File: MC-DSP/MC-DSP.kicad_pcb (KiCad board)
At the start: 2 copper layers, 173 parts, among them J80 5-1634513-1, J81 5-1634513-1, J82 5-1634513-1, SW1 SW_SPDT, U1 TMS320F28388DZWT, U10 ECS-2520MV-xxx-xx, U12 BU4831F-TR, U13 BU4811G-TR, U2 SBH41-NBPB-D10-ST-BK, U20 R-78E3.3-1.0, U200 FT2232HL, U201 TPD2S017, U202 USB_B, U203 AZ1117-3.3, U204 ISO7730DW, U205 ISO7730DW, U206 ISO7730DW, U21 R-78B1.2-2.0, U60 OPA365xxD, U61 OPA365xxD, U62 OPA365xxD, U63 OPA365xxD, U64 OPA365xxD, U65 MAX6126AASA, U80 OPA365xxD, U81 OPA365xxD, U82 OPA365xxD

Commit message: added backplane connector, changed right angle headers, added FP for bigger reg caps, all ICs arranged, routed isolated section.
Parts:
- removed D11, D12: WP1384AD/YD, LED_THT:LED_D3.0mm
- removed R11, R12: 1K, Resistor_SMD:R_0603_1608Metric_Pad0.98x0.95mm_HandSolder
- removed R13: 44R, Resistor_SMD:R_0603_1608Metric_Pad0.98x0.95mm_HandSolder
- removed R14, R15, R16, R17: 10R, Resistor_SMD:R_0603_1608Metric_Pad0.98x0.95mm_HandSolder
- added H2: Conn_01x05, Connector_PinSocket_2.54mm:PinSocket_1x05_P2.54mm_Vertical, F.Cu at (251.2, 23.6)
- added H3: Conn_01x05, Connector_PinSocket_2.54mm:PinSocket_1x05_P2.54mm_Vertical, F.Cu at (253.7, 23.6)
- added J1: 374385, 374385:374385, F.Cu at (113.9, 101.1)
- added U207: Crystal_GND24, Oscillator:Oscillator_SMD_TXC_7C-4Pin_5.0x3.2mm_HandSoldering, F.Cu at (233.6, 105.7)
- C21, C22, C28: footprint Capacitor_SMD:C_0603_1608Metric_Pad1.08x0.95mm_HandSolder -> Capacitor_SMD:C_1210_3225Metric
- H1: value Conn_02x12_Odd_Even -> Conn_01x05; footprint Connector_PinHeader_1.27mm:PinHeader_2x12_P1.27mm_Vertical -> Connector_PinSocket_2.54mm:PinSocket_1x05_P2.54mm_Vertical
- moved U12 391.6 mm to (178.1, 25.1), turned to 270 degrees
- moved C14 384.6 mm to (178.1, 27.7)
- moved C16 378.6 mm to (178.1, 31.2), turned to 180 degrees
- moved R18 377.2 mm to (178.1, 29.5)
- moved U13 369.0 mm to (178.1, 35.3)
- moved C15 362.0 mm to (178.1, 38.6)
- moved R21 351.4 mm to (167.8, 33.2)
- moved R20 349.4 mm to (160.3, 20.0), turned to 180 degrees
- moved U21 346.7 mm to (156.6, 34.6)
- moved C22 345.3 mm to (140.7, 23.0), turned to 270 degrees
- moved L22 345.2 mm to (168.1, 35.4), turned to 180 degrees
- moved C28 344.4 mm to (141.1, 39.1), turned to 90 degrees
- moved C30 344.4 mm to (166.9, 38.6), turned to 90 degrees
- moved C31 344.2 mm to (169.4, 38.6), turned to 270 degrees
- moved L24 342.9 mm to (148.0, 39.3), turned to 90 degrees
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- renumbered TP1 to T1
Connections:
- net /Ethernet/COL renamed Net-(U1-PadM2)
- net /Ethernet/CRS renamed Net-(U1-PadN2)
- net /Ethernet/MDC renamed Net-(U1-PadJ3)
- net /Ethernet/MDIO renamed Net-(U1-PadL2)
- net /Ethernet/PWDN renamed Net-(U1-PadL4)
- net /Ethernet/RX_CLK renamed Net-(U1-PadM4)
- net /Ethernet/RX_D0 renamed Net-(U1-PadN3)
- net /Ethernet/RX_D1 renamed Net-(U1-PadV12)
- net /Ethernet/RX_D2 renamed Net-(U1-PadW10)
- net /Ethernet/RX_D3 renamed Net-(U1-PadU12)
- net /Ethernet/RX_DV renamed Net-(U1-PadM3)
- net /Ethernet/RX_ER renamed Net-(U1-PadN4)
- net /Ethernet/Reset renamed Net-(U1-PadT15)
- net /Ethernet/TX_CLK renamed Net-(U1-PadU15)
- net /Ethernet/TX_D0 renamed Net-(U1-PadW16)
- net /Ethernet/TX_D1 renamed Net-(U1-PadT8)
- net /Ethernet/TX_D2 renamed Net-(U1-PadU8)
- net /Ethernet/TX_D3 renamed Net-(U1-PadV8)
- net /Ethernet/TX_EN renamed Net-(U1-PadT12)
- C13 pad 1: +3V3 -> GND
- C13 pad 2: GND -> +3V3
- C200 pad 2: GND -> EMU_GND
- C201 pad 2: GND -> EMU_GND
- C202 pad 2: GND -> EMU_GND
- C203 pad 2: GND -> EMU_GND
- C204 pad 2: GND -> EMU_GND
- C205 pad 2: GND -> EMU_GND
- C206 pad 2: GND -> EMU_GND
- C207 pad 2: GND -> EMU_GND
- C208 pad 2: GND -> EMU_GND
- C209 pad 2: GND -> EMU_GND
- H1 pad 2: /CLB_OUTPUTX_BAR8 -> /OUTPUTXBAR2
- H1 pad 3: /OUTPUTXBAR2 -> GND
- H1 pad 4: /CLB_OUTPUTX_BAR7 -> /OUTPUTXBAR3
- H1 pad 5: /OUTPUTXBAR3 -> /OUTPUTXBAR4
- R109 pad 1: CLK_25M_DSP -> /25MHz_clk_DSP
- U1 pad G19: CLK_25M_DSP -> /25MHz_clk_DSP
- U10 pad 3: Net-(U10-Pad3) -> /25MHz_clk_DSP
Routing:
- net EMU_GND: track 0.00 -> 53.9 mm, vias 0 -> 26
- net Net-(JP201-Pad2): track 0.00 -> 30.7 mm, vias 0 -> 2
- net EMU_3V3: track 0.00 -> 29.5 mm, vias 0 -> 16
- net /FTDI/EMU_TCK: track 0.00 -> 28.7 mm, vias 0 -> 1
- net /FTDI/EMU_SCI-TX: track 0.00 -> 26.6 mm, vias 0 -> 2
- net /FTDI/EMU_TDI: track 0.00 -> 26.0 mm, vias 0 -> 2
- net Net-(JP200-Pad2): track 0.00 -> 24.3 mm, vias 0 -> 2
- net /FTDI/EMU_TMS: track 0.00 -> 24.0 mm, vias 0 -> 2
- net /FTDI/EMU_SCI-RX: track 0.00 -> 17.0 mm, vias 0 -> 2
- net /FTDI/EMU_TDO: track 0.00 -> 16.4 mm, vias 0 -> 2
- net EMU_1V8: track 0.00 -> 16.0 mm, vias 0 -> 4
- net Net-(R201-Pad1): track 0.00 -> 15.1 mm
- net /FTDI/EMU_TRSTn: track 0.00 -> 11.6 mm, vias 0 -> 2
- net Net-(R205-Pad2): track 0.00 -> 10.4 mm
- net EMU_USB_5V: track 0.00 -> 10.4 mm
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- added copper zone on B.Cu, net EMU_1V8
- added copper zone on In2.Cu, net EMU_3V3
- added copper zone on In3.Cu, net EMU_5V
- added copper zone on In1.Cu, net EMU_GND
- added copper zone on In4.Cu, net EMU_GND
- added copper zone on In1.Cu, net GND
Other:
- board outline added: 160 x 100 mm
- copper layers 2 -> 6
- rule trace_min: 0.2 -> 0.1524
- rule via_min_size: 0.4 -> 0.2032

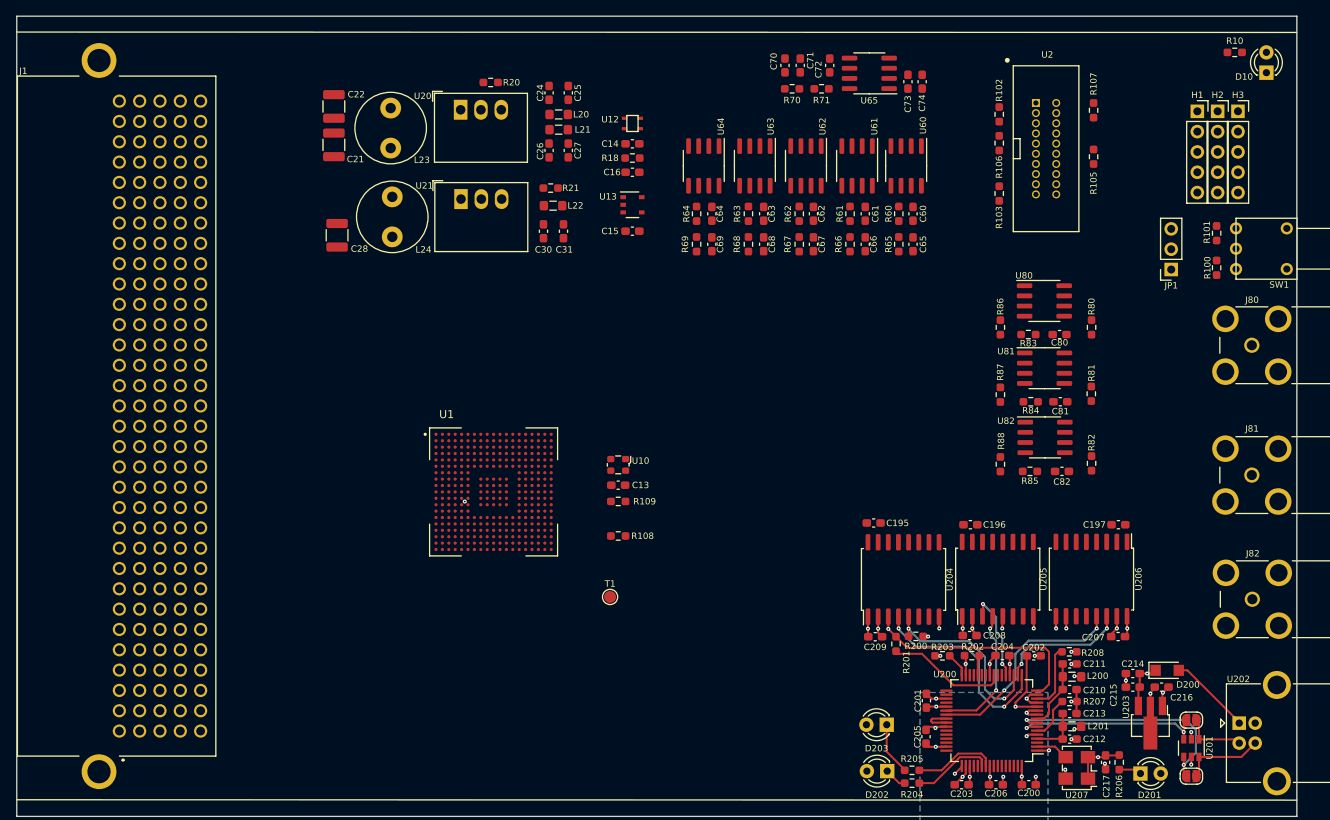
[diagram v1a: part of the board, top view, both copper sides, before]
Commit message: connected DSP signals to BP connector symbol, routed most non-signal traces on PCB
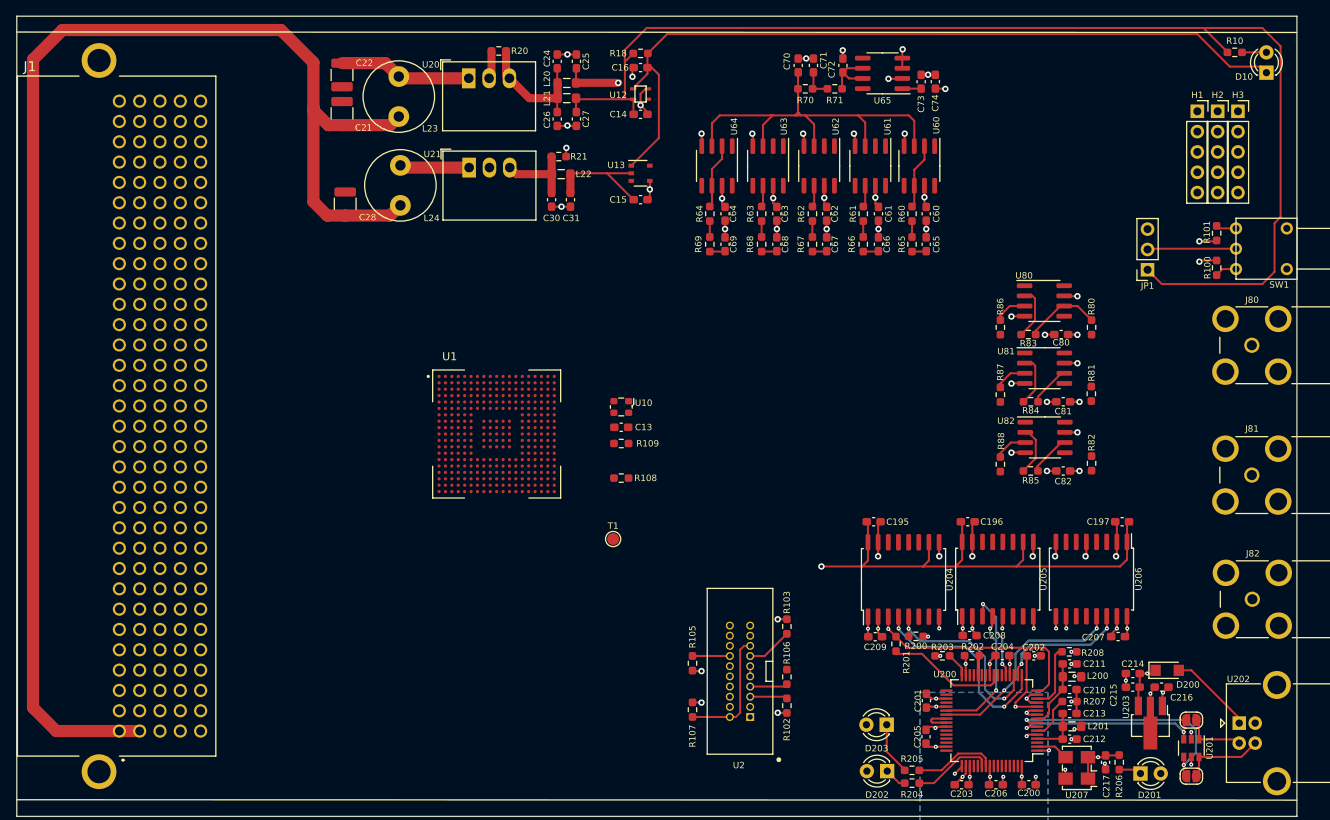
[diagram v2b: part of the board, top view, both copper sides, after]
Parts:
- JP1: value Jumper_3_Bridged12 -> EE_Switch
- moved R107 90.2 mm to (185.6, 98.4), turned to 90 degrees
- moved R105 80.8 mm to (185.6, 92.6), turned to 90 degrees
- moved R102 78.5 mm to (197.4, 97.9), turned to 270 degrees
- moved U2 75.7 mm to (191.5, 93.6), turned to 180 degrees
- moved R106 71.8 mm to (197.4, 94.3), turned to 90 degrees
- moved R103 60.3 mm to (197.4, 88.0), turned to 90 degrees
- moved C16 13.1 mm to (179.1, 18.2)
- moved R18 13.1 mm to (179.1, 16.4)
- moved C13 7.25 mm to (176.7, 63.1)
- moved R108 7.25 mm to (176.7, 69.5)
- moved R109 7.25 mm to (176.7, 65.2)
- moved T1 7.25 mm to (175.6, 77.1)
- moved U1 7.25 mm to (161.1, 64.0)
- moved U10 7.25 mm to (176.7, 60.6)
- moved C28 4.07 mm to (142.2, 35.2)
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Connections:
- J1 pad A1: Net-(J1-PadA1) -> VDD
- J1 pad A10: Net-(J1-PadA10) -> GND
- J1 pad A11: Net-(J1-PadA11) -> GND
- J1 pad A12: Net-(J1-PadA12) -> GND
- J1 pad A13: Net-(J1-PadA13) -> GND
- J1 pad A14: Net-(J1-PadA14) -> GND
- J1 pad A15: Net-(J1-PadA15) -> /SD2_D2
- J1 pad A16: Net-(J1-PadA16) -> GND
- J1 pad A17: Net-(J1-PadA17) -> /GPIO14
- J1 pad A18: Net-(J1-PadA18) -> GND
- J1 pad A19: Net-(J1-PadA19) -> /GPIO16
- J1 pad A2: Net-(J1-PadA2) -> GND
- J1 pad A20: Net-(J1-PadA20) -> GND
- J1 pad A21: Net-(J1-PadA21) -> /EPWM3A
- J1 pad A22: Net-(J1-PadA22) -> GND
- J1 pad A23: Net-(J1-PadA23) -> /EPWM5B
- J1 pad A24: Net-(J1-PadA24) -> GND
- J1 pad A25: Net-(J1-PadA25) -> /GPIO24
- J1 pad A26: Net-(J1-PadA26) -> GND
- J1 pad A27: Net-(J1-PadA27) -> /EPWM8A
- J1 pad A28: Net-(J1-PadA28) -> GND
- J1 pad A29: Net-(J1-PadA29) -> /EPWM10B
- J1 pad A3: Net-(J1-PadA3) -> /ADC_C3
- J1 pad A30: Net-(J1-PadA30) -> GND
- J1 pad A31: Net-(J1-PadA31) -> /EPWM12A
- J1 pad A32: Net-(J1-PadA32) -> GND
- J1 pad A4: Net-(J1-PadA4) -> GND
- J1 pad A5: Net-(J1-PadA5) -> /ADC_A2
- J1 pad A6: Net-(J1-PadA6) -> GND
- J1 pad A7: Net-(J1-PadA7) -> /ADC_A5
- J1 pad A8: Net-(J1-PadA8) -> GND
- J1 pad A9: Net-(J1-PadA9) -> /ADC_B4
- J1 pad B1: Net-(J1-PadB1) -> VDD
- J1 pad B10: Net-(J1-PadB10) -> GND
- J1 pad B11: Net-(J1-PadB11) -> GND
- J1 pad B12: Net-(J1-PadB12) -> /SD1_D4
- J1 pad B13: Net-(J1-PadB13) -> GND
- J1 pad B14: Net-(J1-PadB14) -> GND
- J1 pad B15: Net-(J1-PadB15) -> GND
- J1 pad B16: Net-(J1-PadB16) -> /EPWM13A
- J1 pad B17: Net-(J1-PadB17) -> GND
- J1 pad B18: Net-(J1-PadB18) -> /GPIO15
- J1 pad B19: Net-(J1-PadB19) -> GND
- J1 pad B2: Net-(J1-PadB2) -> GND
- J1 pad B20: Net-(J1-PadB20) -> /EPWM2A
- J1 pad B21: Net-(J1-PadB21) -> GND
- J1 pad B22: Net-(J1-PadB22) -> /EPWM4B
- J1 pad B23: Net-(J1-PadB23) -> GND
- J1 pad B24: Net-(J1-PadB24) -> /GPIO23
- J1 pad B25: Net-(J1-PadB25) -> GND
- J1 pad B26: Net-(J1-PadB26) -> /EPWM7A
- J1 pad B27: Net-(J1-PadB27) -> GND
- J1 pad B28: Net-(J1-PadB28) -> /EPWM9B
- J1 pad B29: Net-(J1-PadB29) -> GND
- J1 pad B3: Net-(J1-PadB3) -> GND
- J1 pad B30: Net-(J1-PadB30) -> /GPIO52
- J1 pad B31: Net-(J1-PadB31) -> GND
- J1 pad B32: Net-(J1-PadB32) -> /EPWM12B
- J1 pad B4: Net-(J1-PadB4) -> /ADC_B2
- J1 pad B5: Net-(J1-PadB5) -> GND
- J1 pad B6: Net-(J1-PadB6) -> /ADC_C5
- J1 pad B7: Net-(J1-PadB7) -> GND
- J1 pad B8: Net-(J1-PadB8) -> /ADC_D2
- J1 pad B9: Net-(J1-PadB9) -> GND
- J1 pad C1: Net-(J1-PadC1) -> GND
- J1 pad C10: Net-(J1-PadC10) -> GND
- J1 pad C11: Net-(J1-PadC11) -> /SD1_D2
- J1 pad C12: Net-(J1-PadC12) -> GND
- J1 pad C13: Net-(J1-PadC13) -> /EPWM14A
- J1 pad C14: Net-(J1-PadC14) -> GND
- J1 pad C15: Net-(J1-PadC15) -> /SD2_D4
- J1 pad C16: Net-(J1-PadC16) -> GND
- J1 pad C17: Net-(J1-PadC17) -> /Emitter_Enable
- J1 pad C18: Net-(J1-PadC18) -> GND
- J1 pad C19: Net-(J1-PadC19) -> /EPWM1A
- J1 pad C2: Net-(J1-PadC2) -> GND
- J1 pad C20: Net-(J1-PadC20) -> GND
- J1 pad C21: Net-(J1-PadC21) -> /EPWM3B
- J1 pad C22: Net-(J1-PadC22) -> GND
- J1 pad C23: Net-(J1-PadC23) -> /GPIO22
- J1 pad C24: Net-(J1-PadC24) -> GND
- J1 pad C25: Net-(J1-PadC25) -> /EPWM6A
- J1 pad C26: Net-(J1-PadC26) -> GND
- J1 pad C27: Net-(J1-PadC27) -> /EPWM8B
- J1 pad C28: Net-(J1-PadC28) -> GND
- J1 pad C29: Net-(J1-PadC29) -> /GPIO45
- J1 pad C3: Net-(J1-PadC3) -> /ADC_C2
- J1 pad C30: Net-(J1-PadC30) -> GND
- J1 pad C31: Net-(J1-PadC31) -> /EPWM11A
- J1 pad C32: Net-(J1-PadC32) -> GND
- J1 pad C4: Net-(J1-PadC4) -> GND
- J1 pad C5: Net-(J1-PadC5) -> /ADC_D1
- J1 pad C6: Net-(J1-PadC6) -> GND
- J1 pad C7: Net-(J1-PadC7) -> /ADC_A4
- J1 pad C8: Net-(J1-PadC8) -> GND
- J1 pad C9: Net-(J1-PadC9) -> /ADC_15
- J1 pad D1: Net-(J1-PadD1) -> GND
- J1 pad D10: Net-(J1-PadD10) -> GND
- J1 pad D11: Net-(J1-PadD11) -> GND
- J1 pad D12: Net-(J1-PadD12) -> /SD1_D3
- J1 pad D13: Net-(J1-PadD13) -> GND
- J1 pad D14: Net-(J1-PadD14) -> /SD2_D1
- J1 pad D15: Net-(J1-PadD15) -> GND
- J1 pad D16: Net-(J1-PadD16) -> GND
- J1 pad D17: Net-(J1-PadD17) -> GND
- J1 pad D18: Net-(J1-PadD18) -> GND
- J1 pad D19: Net-(J1-PadD19) -> GND
- J1 pad D2: Net-(J1-PadD2) -> GND
- J1 pad D20: Net-(J1-PadD20) -> /EPWM2B
- J1 pad D21: Net-(J1-PadD21) -> GND
- J1 pad D22: Net-(J1-PadD22) -> /GPIO19
- J1 pad D23: Net-(J1-PadD23) -> GND
- J1 pad D24: Net-(J1-PadD24) -> /EPWM5A
- J1 pad D25: Net-(J1-PadD25) -> GND
- J1 pad D26: Net-(J1-PadD26) -> /EPWM7B
- J1 pad D27: Net-(J1-PadD27) -> GND
- J1 pad D28: Net-(J1-PadD28) -> /GPIO44
- J1 pad D29: Net-(J1-PadD29) -> GND
- J1 pad D3: Net-(J1-PadD3) -> GND
- J1 pad D30: Net-(J1-PadD30) -> /EPWM10A
- J1 pad D31: Net-(J1-PadD31) -> GND
- J1 pad D32: Net-(J1-PadD32) -> /GPIO53
- J1 pad D4: Net-(J1-PadD4) -> /ADC_A3
- J1 pad D5: Net-(J1-PadD5) -> GND
- J1 pad D6: Net-(J1-PadD6) -> /ADC_C4
- J1 pad D7: Net-(J1-PadD7) -> GND
- J1 pad D8: Net-(J1-PadD8) -> /ADC_B5
- J1 pad D9: Net-(J1-PadD9) -> GND
- J1 pad E1: Net-(J1-PadE1) -> GND
- J1 pad E10: Net-(J1-PadE10) -> GND
- J1 pad E11: Net-(J1-PadE11) -> /SD1_D1
- J1 pad E12: Net-(J1-PadE12) -> GND
- J1 pad E13: Net-(J1-PadE13) -> GND
- J1 pad E14: Net-(J1-PadE14) -> GND
- J1 pad E15: Net-(J1-PadE15) -> /SD2_D3
- J1 pad E16: Net-(J1-PadE16) -> GND
- J1 pad E17: Net-(J1-PadE17) -> /Safe_State
- J1 pad E18: Net-(J1-PadE18) -> GND
- J1 pad E19: Net-(J1-PadE19) -> /EPWM1B
- J1 pad E2: Net-(J1-PadE2) -> GND
- J1 pad E20: Net-(J1-PadE20) -> GND
- J1 pad E21: Net-(J1-PadE21) -> /GPIO18
- J1 pad E22: Net-(J1-PadE22) -> GND
- J1 pad E23: Net-(J1-PadE23) -> /EPWM4A
- J1 pad E24: Net-(J1-PadE24) -> GND
- J1 pad E25: Net-(J1-PadE25) -> /EPWM6B
- J1 pad E26: Net-(J1-PadE26) -> GND
- J1 pad E27: Net-(J1-PadE27) -> /GPIO25
- J1 pad E28: Net-(J1-PadE28) -> GND
- J1 pad E29: Net-(J1-PadE29) -> /EPWM9A
- J1 pad E3: Net-(J1-PadE3) -> /ADC_B3
- J1 pad E30: Net-(J1-PadE30) -> GND
- J1 pad E31: Net-(J1-PadE31) -> /EPWM11B
- J1 pad E32: Net-(J1-PadE32) -> GND
- J1 pad E4: Net-(J1-PadE4) -> GND
- J1 pad E5: Net-(J1-PadE5) -> /ADC_D0
- J1 pad E6: Net-(J1-PadE6) -> GND
- J1 pad E7: Net-(J1-PadE7) -> /ADC_D3
- J1 pad E8: Net-(J1-PadE8) -> GND
- J1 pad E9: Net-(J1-PadE9) -> /ADC_14
- JP1 pad 1: Emitter_Enable_DSP -> +3V3
- JP1 pad 3: +3V3 -> Net-(JP1-Pad3)
- R101 pad 1: Emitter_Enable_Backplane -> /Emitter_Enable
- SW1 pad 1: Emitter_Enable_Backplane -> /Emitter_Enable
- U1 pad C2: Net-(U1-PadC2) -> Net-(JP1-Pad3)
- U1 pad D2: Net-(U1-PadD2) -> /GPIO14
- U1 pad D3: Net-(U1-PadD3) -> /GPIO15
- U1 pad E1: Net-(U1-PadE1) -> /GPIO16
- U1 pad E3: Net-(U1-PadE3) -> /GPIO18
- U1 pad E4: Net-(U1-PadE4) -> /GPIO19
- U1 pad J4: Net-(U1-PadJ4) -> /GPIO22
- U1 pad K18: Net-(U1-PadK18) -> /GPIO44
- U1 pad K19: Net-(U1-PadK19) -> /GPIO45
- U1 pad K2: Net-(U1-PadK2) -> /GPIO25
- U1 pad K3: Net-(U1-PadK3) -> /GPIO24
- U1 pad K4: Net-(U1-PadK4) -> /GPIO23
- U1 pad P16: Net-(U1-PadP16) -> /GPIO52
- U1 pad P17: Net-(U1-PadP17) -> /GPIO53
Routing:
- net +3V3: track 0.00 -> 218.1 mm, vias 0 -> 4
- net VDD: track 0.00 -> 175.6 mm
- net /Safe_State: track 0.00 -> 100.0 mm
- net GND: track 0.00 -> 79.5 mm, vias 0 -> 37
- net Net-(C70-Pad2): track 0.00 -> 51.6 mm
- net VDDA: track 0.00 -> 32.6 mm, vias 0 -> 14
- net Net-(C24-Pad2): track 0.00 -> 17.0 mm
- net Net-(C22-Pad1): track 0.00 -> 16.6 mm
- net /NSRST: track 0.00 -> 15.5 mm
- net +1V2: track 0.00 -> 14.7 mm
- net Net-(JP1-Pad2): track 0.00 -> 11.1 mm
- net Net-(C30-Pad2): track 0.00 -> 10.2 mm
- net Net-(R80-Pad2): track 0.00 -> 9.47 mm
- net Net-(L24-Pad2): track 0.00 -> 8.70 mm
- net Net-(R60-Pad1): track 0.00 -> 8.19 mm
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- added copper zone on In2.Cu, net +3V3
- added copper zone on In4.Cu, net GND
- added copper zone on In2.Cu, net VDDA
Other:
- board text added: "Mark Qs: how many layers? how to do layer stackup? how to fit vias under the dsp? what to do about DSP Caps?"
